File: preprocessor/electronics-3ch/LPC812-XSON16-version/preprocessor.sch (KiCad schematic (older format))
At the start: 11 parts, among them P1 ST-IN, P2 ST-OUT, P3 TH-IN, P4 TH-OUT, P5 AUX-IN, P6 LIGHT CONTROLLER, U1 MCP1703T-3302E/CB, U2 LPC811M001JDH16_TSSOP16

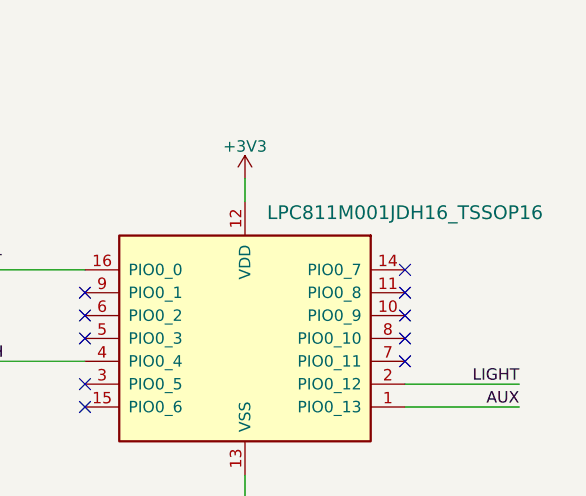
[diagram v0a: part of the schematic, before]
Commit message: Streamline gerber filenames and add schematics PDF everywhere
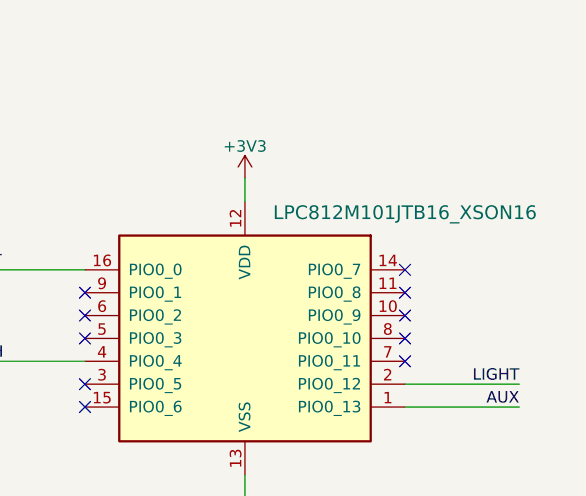
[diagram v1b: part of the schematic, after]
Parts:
- U2: value LPC811M001JDH16_TSSOP16 -> LPC812M101JTB16_XSON16
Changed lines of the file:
@@
 P 7300 2550
 F 0 "U2" H 7200 2650 10  0001 C CNN
-F 1 "LPC811M001JDH16_TSSOP16" H 8000 3100 60  0000 C CNN
+F 1 "LPC812M101JTB16_XSON16" H 8000 3100 60  0000 C CNN
 F 2 "Package_SON:NXP_XSON-16" H 7200 2650 60  0001 C CNN
 F 3 "" H 7200 2650 60  0000 C CNN
